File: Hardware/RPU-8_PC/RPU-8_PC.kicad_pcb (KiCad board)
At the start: 4 copper layers, 139.7 x 55.9 mm, 10 parts, among them J1 ADDR_BUS, J2 DATA_BUS, J3 Conn_01x03_Female, J4 CTRL_BUS, U1 74HC161, U2 74HC245, U3 74HC161, U4 74HC161, U5 74HC245, U6 74HC161

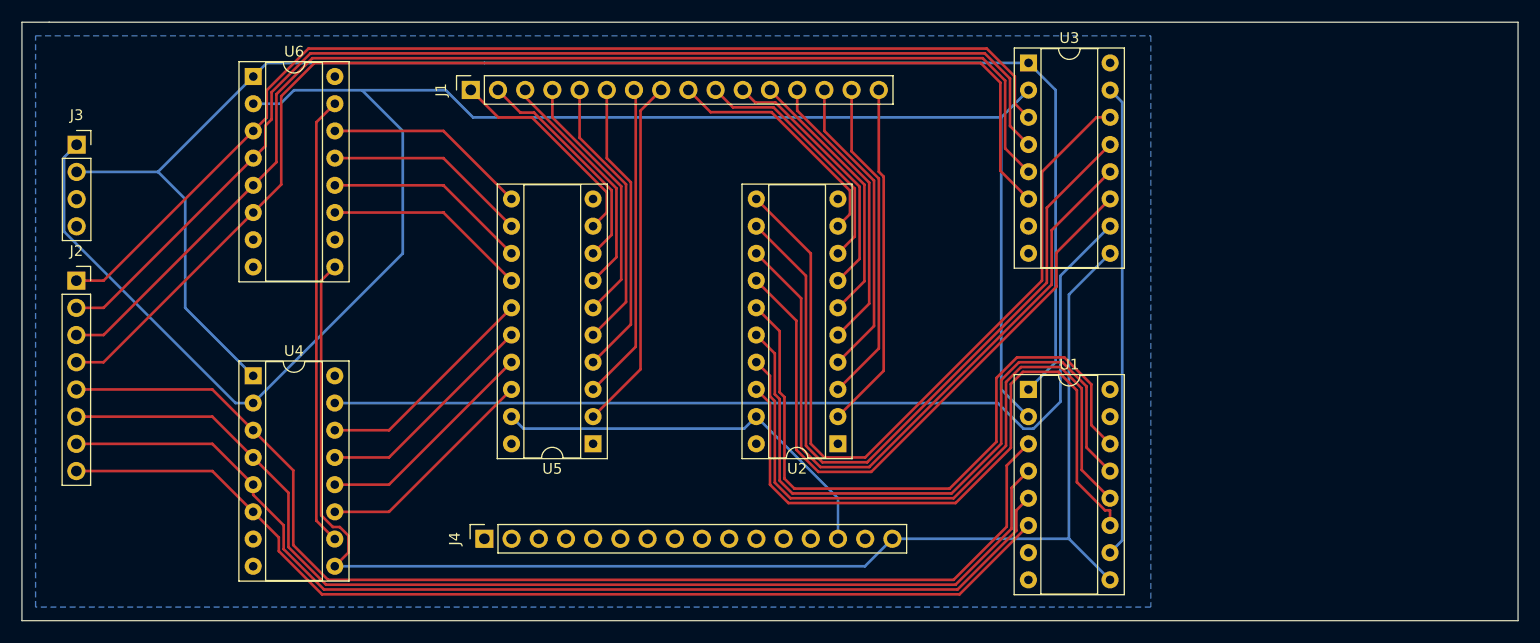
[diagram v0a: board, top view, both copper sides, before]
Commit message: new 8-bit PC, add 16-bit later
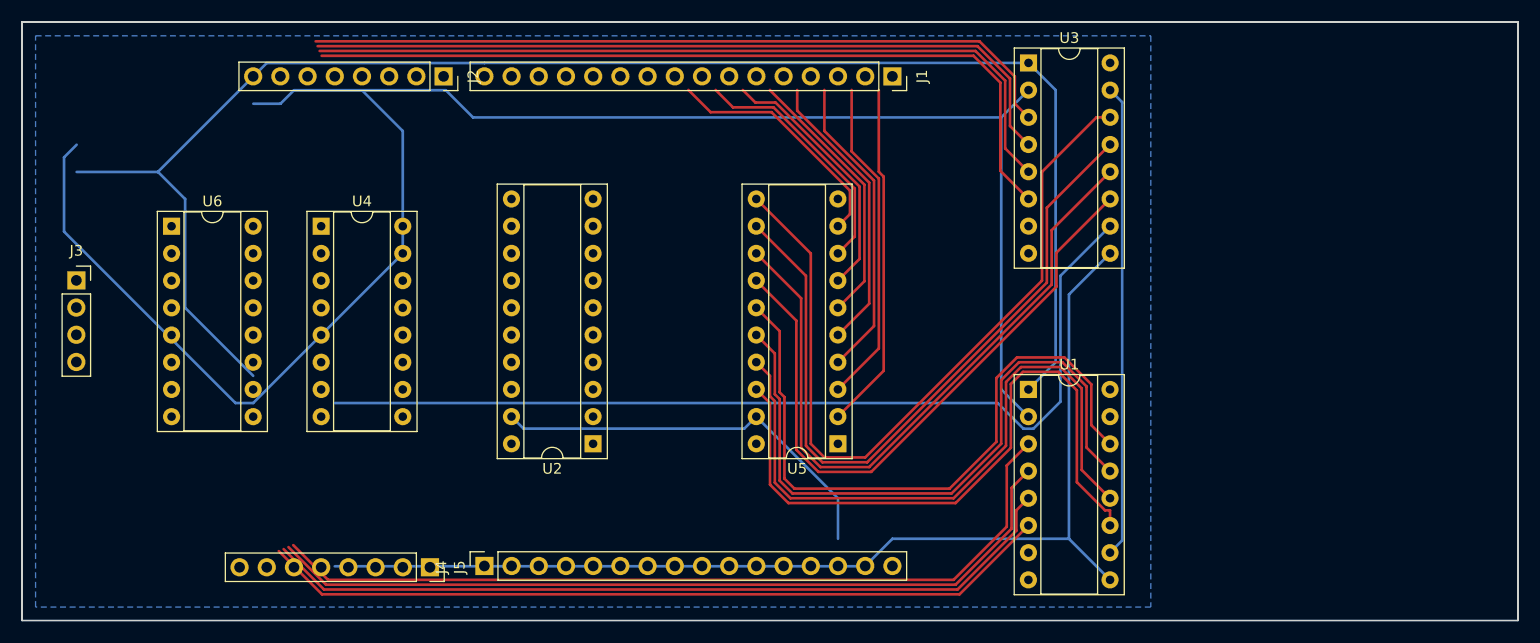
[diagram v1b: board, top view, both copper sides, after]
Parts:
- added J5: INST_REG, Connector_PinSocket_2.54mm:PinSocket_1x08_P2.54mm_Vertical, F.Cu at (106.7, 119.5)
- moved J1 39.4 mm to (149.9, 73.6), turned to -90 degrees
- moved J2 39.2 mm to (108.0, 73.6), turned to -90 degrees
- moved U2 22.9 mm to (121.9, 107.9)
- moved U5 22.9 mm to (144.8, 107.9)
- moved U6 15.9 mm to (82.5, 87.6)
- moved U4 15.3 mm to (96.5, 87.6)
- moved J3 12.7 mm to (73.7, 92.7)
- moved J4 2.54 mm to (111.8, 119.4)
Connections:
- J4 pad 1: ~{CIH} -> (no net)
- J4 pad 16: ~{CIL} -> (no net)
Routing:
- net Net-(U4-Pad10): track 42.1 -> 0.00 mm
- net D3: track 115.4 -> 76.4 mm
- net D2: track 111.4 -> 74.6 mm
- net D1: track 107.5 -> 72.8 mm
- net D0: track 103.5 -> 71.0 mm
- net A15: track 32.5 -> 0.00 mm
- net A14: track 30.6 -> 0.00 mm
- net ~{CIL}: track 133.7 -> 103.3 mm
- net D4: track 109.0 -> 78.6 mm
- net A13: track 28.7 -> 0.00 mm
- net D5: track 105.0 -> 77.2 mm
- net A12: track 26.9 -> 0.00 mm
- net D6: track 101.0 -> 75.8 mm
- net A11: track 25.0 -> 0.00 mm
- net A10: track 24.3 -> 0.00 mm
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
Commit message: add .readthedocs.yaml
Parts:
- moved U1 62.7 mm to (102.9, 83.8), turned to -90 degrees
- moved U6 46.6 mm to (127.0, 101.6), turned to -90 degrees
- moved U3 37.4 mm to (127.0, 83.8), turned to -90 degrees
- moved U2 20.1 mm to (133.4, 91.4), turned to 90 degrees
- moved U4 15.3 mm to (102.9, 101.6), turned to -90 degrees
- moved U5 11.5 mm to (133.3, 109.2), turned to 90 degrees
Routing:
- net +5V: track 0.00 -> 161.4 mm, vias 0 -> 1
- net GND: track 0.00 -> 111.9 mm, vias 0 -> 1
- net CLK: track 173.5 -> 73.3 mm
- net Net-(U3-Pad10): track 88.1 -> 26.0 mm, vias 0 -> 1
- net RST: track 148.4 -> 91.7 mm, vias 0 -> 3
- net Net-(U4-Pad12): track 0.00 -> 51.4 mm
- net Net-(U4-Pad14): track 0.00 -> 51.4 mm
- net Net-(U4-Pad13): track 0.00 -> 51.4 mm
- net Net-(U4-Pad11): track 0.00 -> 51.4 mm
- net D4: track 78.6 -> 29.0 mm
- net D5: track 77.2 -> 29.0 mm
- net D6: track 75.8 -> 29.0 mm
- net D7: track 74.3 -> 29.0 mm
- net A7: track 32.5 -> 74.9 mm
- net ~{CIL}: track 103.3 -> 62.0 mm
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- removed copper zone on In2.Cu, net +5V
- removed copper zone on B.Cu, net GND
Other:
- board size 139.7 x 55.9 mm -> 106.7 x 55.9 mm
- copper layers 4 -> 2
